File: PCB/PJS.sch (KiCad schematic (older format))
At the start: 40 parts, among them J1 HFW8R-1STE1H1LF_FFC, J10 SM02B-PASS-TBT_SwitchConnector, J2 SM02B-PASS-TBT_Connector, J3 SM02B-PASS-TBT_Connector, J4 SM02B-PASS-TBT_Connector, J5 SM02B-PASS-TBT_Connector, J6 SM02B-PASS-TBT_SwitchConnector, J7 SM02B-PASS-TBT_SwitchConnector, J8 SM02B-PASS-TBT_SwitchConnector, J9 SM02B-PASS-TBT_SwitchConnector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

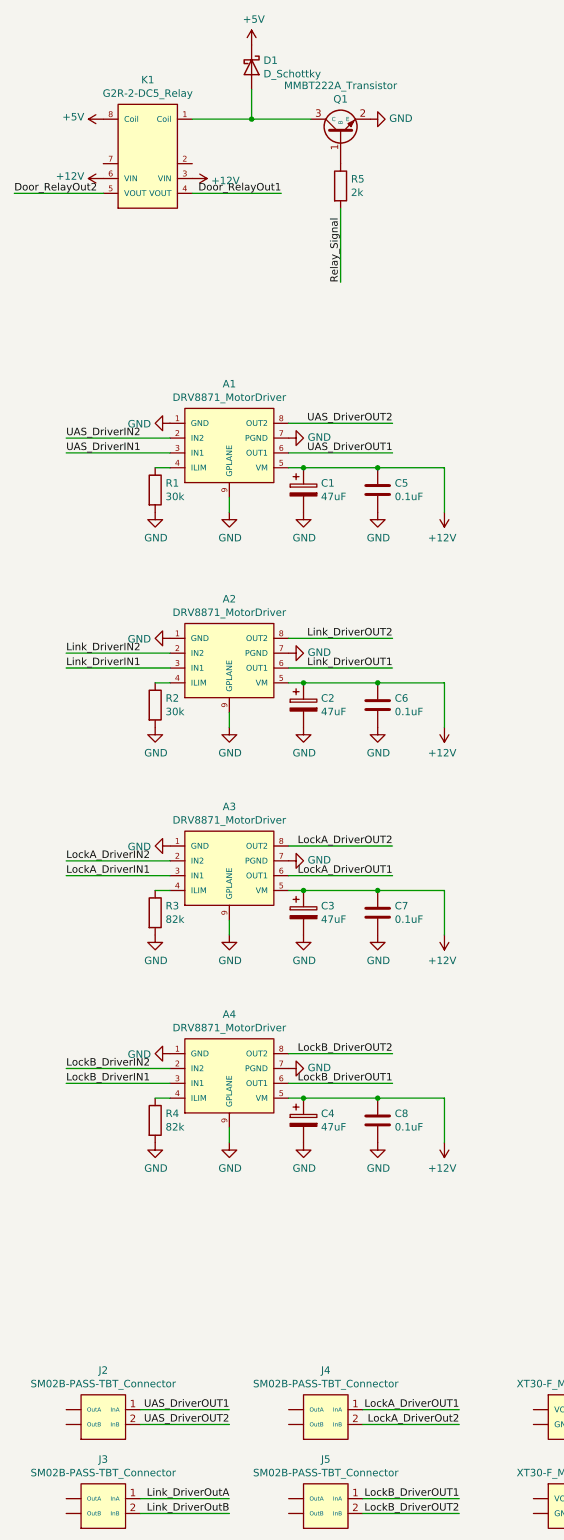
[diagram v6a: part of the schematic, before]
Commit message: Updated DRV8871 footprint
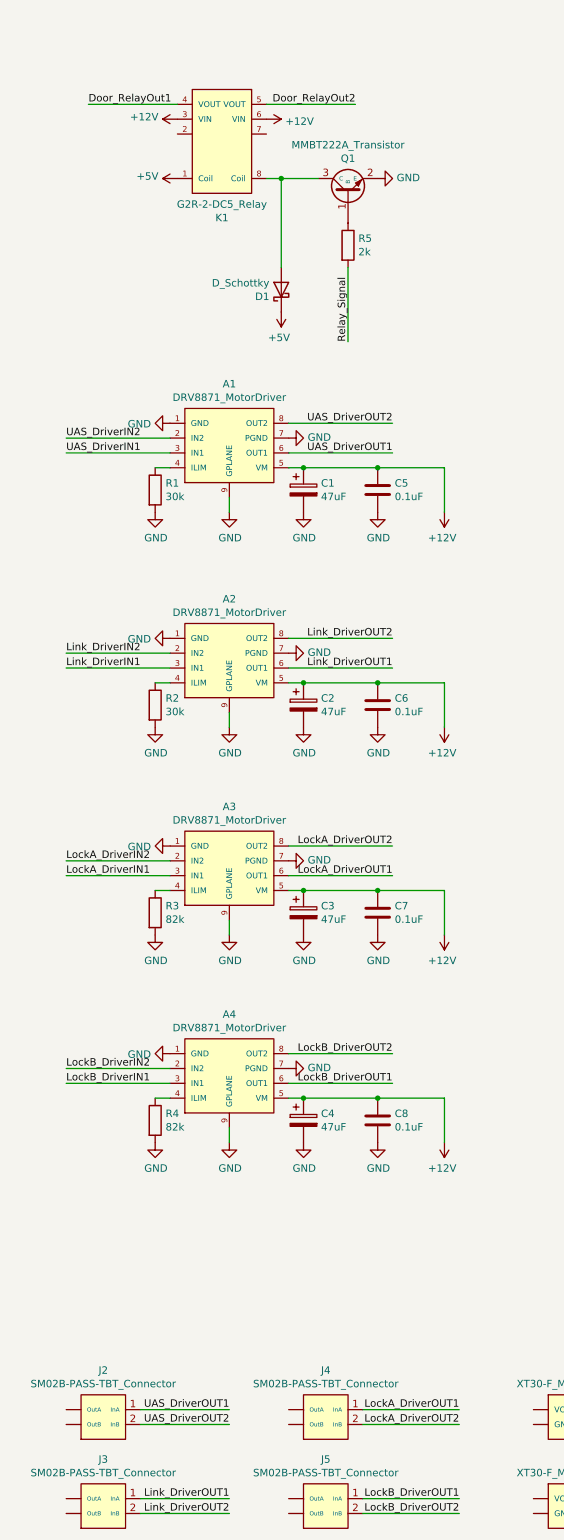
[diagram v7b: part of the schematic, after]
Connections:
- net Link_DriverOutA is gone; now on net Link_DriverOUT1: J3.1 (InA)
- net Link_DriverOutB is gone; now on net Link_DriverOUT2: J3.2 (InB)
- net LockA_DriverOut2 is gone; now on net LockA_DriverOUT2: J4.2 (InB)
- net +5V: now also K1.1 (Coil); no longer K1.8 (Coil)
- net at D1.2 (A), Q1.3 (C): now also K1.8 (Coil); no longer K1.1 (Coil)
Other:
- moved on the sheet: D1, K1, Q1, R5
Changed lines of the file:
@@
-	1    0    0    -1
-$EndComp
-$Comp
-L PJS:G2R-2-DC5_Relay K1
-U 1 1 5FCA000B
-P 1700 1950
-F 0 "K1" H 1700 2715 50  0000 C CNN
-F 1 "G2R-2-DC5_Relay" H 1700 2624 50  0000 C CNN
-F 2 "PJS:G2R-2-DC5_Relay" H 1700 2650 50  0001 C CNN
-F 3 "" H 1700 2650 50  0001 C CNN
-	1    1700 1950
 	1    0    0    -1
 $EndComp
@@
 Wire Wire Line
 	8300 8850 8800 8850
-$Comp
-L power:+12V #PWR0111
-U 1 1 5FF56403
-P 2000 1850
-F 0 "#PWR0111" H 2000 1700 50  0001 C CNN
-F 1 "+12V" V 2015 1978 50  0000 L CNN
-F 2 "" H 2000 1850 50  0001 C CNN
-F 3 "" H 2000 1850 50  0001 C CNN
-	1    2000 1850
-	0    1    1    0
-$EndComp
-$Comp
-L power:+12V #PWR0112
-U 1 1 5FF568D5
-P 1400 1850
-F 0 "#PWR0112" H 1400 1700 50  0001 C CNN
-F 1 "+12V" V 1415 1978 50  0000 L CNN
-F 2 "" H 1400 1850 50  0001 C CNN
-F 3 "" H 1400 1850 50  0001 C CNN
-	1    1400 1850
-	0    -1   -1   0
-$EndComp
 Text Label 2250 10150 2    50   ~ 0
 UAS_DriverOUT1
@@
 UAS_DriverIN2
 Text Label 2250 10750 2    50   ~ 0
-Link_DriverOutA
+Link_DriverOUT1
 Text Label 2250 10850 2    50   ~ 0
-Link_DriverOutB
+Link_DriverOUT2
 $Comp
 L power:+5V #PWR0113
@@
 Wire Wire Line
 	1650 10850 2250 10850
-Text Label 3000 2550 1    50   ~ 0
-Relay_Signal
-Wire Wire Line
-	2400 1250 2400 1450
-Wire Wire Line
-	2000 1450 2400 1450
-Connection ~ 2400 1450
 Wire Wire Line
 	6900 5650 7450 5650
@@
 Wire Wire Line
 	6900 3250 7450 3250
-$Comp
-L Device:D_Schottky D1
-U 1 1 5FFF832A
-P 2400 1100
-F 0 "D1" V 2354 1180 50  0000 L CNN
-F 1 "D_Schottky" V 2445 1180 50  0000 L CNN
-F 2 "PJS:1SS351-TB-E_Diode" H 2400 1100 50  0001 C CNN
-F 3 "~" H 2400 1100 50  0001 C CNN
-	1    2400 1100
-	0    1    1    0
-$EndComp
-$Comp
-L PJS:R R5
-U 1 1 5FFF9163
-P 3000 1900
-F 0 "R5" H 3070 1946 50  0000 L CNN
-F 1 "2k" H 3070 1855 50  0000 L CNN
-F 2 "PJS:RMCF2512FT2K00_Resistor" V 2930 1900 50  0001 C CNN
-F 3 "~" H 3000 1900 50  0001 C CNN
-	1    3000 1900
-	1    0    0    -1
-$EndComp
-Text Label 2600 1950 2    50   ~ 0
-Door_RelayOut1
-Text Label 800  1950 0    50   ~ 0
-Door_RelayOut2
-Wire Wire Line
-	2000 1950 2600 1950
-Wire Wire Line
-	800  1950 1400 1950
 $Comp
 L power:GND #PWR0117
@@
 LockA_DriverOUT1
 Text Label 3800 10250 2    50   ~ 0
-LockA_DriverOut2
+LockA_DriverOUT2
 Text Label 3800 10750 2    50   ~ 0
 LockB_DriverOUT1
 Text Label 3800 10850 2    50   ~ 0
 LockB_DriverOUT2
-Wire Wire Line
-	3000 2050 3000 2550
 Text Label 6450 4450 2    50   ~ 0
 S2_Door
@@
 Wire Wire Line
 	6450 3250 6450 3850
-Wire Wire Line
-	2400 1450 2800 1450
-$Comp
-L PJS:MMBT222A_Transistor Q1
-U 1 1 5FEF3CA0
-P 3000 1500
-F 0 "Q1" V 3185 1500 50  0000 C CNN
-F 1 "MMBT222A_Transistor" V 3276 1500 50  0000 C CNN
-F 2 "PJS:MMBT2222A_Transistor" H 3000 2100 50  0001 C CNN
-F 3 "" H 3000 2100 50  0001 C CNN
-	1    3000 1500
-	0    -1   -1   0
-$EndComp
-$Comp
-L power:GND #PWR0122
-U 1 1 5FF68CB5
-P 3200 1450
-F 0 "#PWR0122" H 3200 1200 50  0001 C CNN
-F 1 "GND" V 3205 1322 50  0000 R CNN
-F 2 "" H 3200 1450 50  0001 C CNN
-F 3 "" H 3200 1450 50  0001 C CNN
-	1    3200 1450
-	0    -1   -1   0
-$EndComp
 $Comp
 L PJS:BMP388_Altimeter A5
@@
 $EndComp
 $Comp
-L power:+5V #PWR0154
-U 1 1 5FF0C5F2
-P 2400 950
-F 0 "#PWR0154" H 2400 800 50  0001 C CNN
-F 1 "+5V" H 2415 1123 50  0000 C CNN
-F 2 "" H 2400 950 50  0001 C CNN
-F 3 "" H 2400 950 50  0001 C CNN
-	1    2400 950
-	1    0    0    -1
-$EndComp
-$Comp
-L power:+5V #PWR0155
-U 1 1 5FF0D0F3
-P 1400 1450
-F 0 "#PWR0155" H 1400 1300 50  0001 C CNN
-F 1 "+5V" V 1415 1578 50  0000 L CNN
-F 2 "" H 1400 1450 50  0001 C CNN
-F 3 "" H 1400 1450 50  0001 C CNN
-	1    1400 1450
-	0    -1   -1   0
-$EndComp
-$Comp
 L PJS:DRV8871_MotorDriver A1
 U 1 1 5FF34B84
@@
 Text Label 6900 3950 0    50   ~ 0
 LockB_DriverIN2
+$Comp
+L PJS:G2R-2-DC5_Relay K1
+U 1 1 5FCA000B
+P 2200 1350
+F 0 "K1" H 2200 2115 50  0000 C CNN
+F 1 "G2R-2-DC5_Relay" H 2200 2024 50  0000 C CNN
+F 2 "PJS:G2R-2-DC5_Relay" H 2200 2050 50  0001 C CNN
+F 3 "" H 2200 2050 50  0001 C CNN
+	1    2200 1350
+	-1   0    0    1
+$EndComp
+$Comp
+L power:+12V #PWR0111
+U 1 1 5FF56403
+P 1900 1450
+F 0 "#PWR0111" H 1900 1300 50  0001 C CNN
+F 1 "+12V" V 1915 1578 50  0000 L CNN
+F 2 "" H 1900 1450 50  0001 C CNN
+F 3 "" H 1900 1450 50  0001 C CNN
+	1    1900 1450
+	0    -1   -1   0
+$EndComp
+$Comp
+L power:+12V #PWR0112
+U 1 1 5FF568D5
+P 2500 1450
+F 0 "#PWR0112" H 2500 1300 50  0001 C CNN
+F 1 "+12V" V 2515 1578 50  0000 L CNN
+F 2 "" H 2500 1450 50  0001 C CNN
+F 3 "" H 2500 1450 50  0001 C CNN
+	1    2500 1450
+	0    1    1    0
+$EndComp
+Text Label 1300 1350 0    50   ~ 0
+Door_RelayOut1
+Wire Wire Line
+	1900 1350 1300 1350
+$Comp
+L power:+5V #PWR0155
+U 1 1 5FF0D0F3
+P 1900 1850
+F 0 "#PWR0155" H 1900 1700 50  0001 C CNN
+F 1 "+5V" V 1915 1978 50  0000 L CNN
+F 2 "" H 1900 1850 50  0001 C CNN
+F 3 "" H 1900 1850 50  0001 C CNN
+	1    1900 1850
+	0    -1   -1   0
+$EndComp
+$Comp
+L power:+5V #PWR0154
+U 1 1 5FF0C5F2
+P 2600 2750
+F 0 "#PWR0154" H 2600 2600 50  0001 C CNN
+F 1 "+5V" H 2615 2923 50  0000 C CNN
+F 2 "" H 2600 2750 50  0001 C CNN
+F 3 "" H 2600 2750 50  0001 C CNN
+	1    2600 2750
+	-1   0    0    1
+$EndComp
+$Comp
+L power:GND #PWR0122
+U 1 1 5FF68CB5
+P 3250 1850
+F 0 "#PWR0122" H 3250 1600 50  0001 C CNN
+F 1 "GND" V 3255 1722 50  0000 R CNN
+F 2 "" H 3250 1850 50  0001 C CNN
+F 3 "" H 3250 1850 50  0001 C CNN
+	1    3250 1850
+	0    -1   -1   0
+$EndComp
+Wire Wire Line
+	3100 1350 2500 1350
+Text Label 3100 1350 2    50   ~ 0
+Door_RelayOut2
+Wire Wire Line
+	3050 2450 3050 2950
+$Comp
+L PJS:R R5
+U 1 1 5FFF9163
+P 3050 2300
+F 0 "R5" H 3120 2346 50  0000 L CNN
+F 1 "2k" H 3120 2255 50  0000 L CNN
+F 2 "PJS:RMCF2512FT2K00_Resistor" V 2980 2300 50  0001 C CNN
+F 3 "~" H 3050 2300 50  0001 C CNN
+	1    3050 2300
+	1    0    0    -1
+$EndComp
+Text Label 3050 2950 1    50   ~ 0
+Relay_Signal
+$Comp
+L PJS:MMBT222A_Transistor Q1
+U 1 1 5FEF3CA0
+P 3050 1900
+F 0 "Q1" V 3235 1900 50  0000 C CNN
+F 1 "MMBT222A_Transistor" V 3326 1900 50  0000 C CNN
+F 2 "PJS:MMBT2222A_Transistor" H 3050 2500 50  0001 C CNN
+F 3 "" H 3050 2500 50  0001 C CNN
+	1    3050 1900
+	0    -1   -1   0
+$EndComp
+$Comp
+L Device:D_Schottky D1
+U 1 1 5FFF832A
+P 2600 2600
+F 0 "D1" V 2554 2680 50  0000 L CNN
+F 1 "D_Schottky" V 2645 2680 50  0000 L CNN
+F 2 "PJS:1SS351-TB-E_Diode" H 2600 2600 50  0001 C CNN
+F 3 "~" H 2600 2600 50  0001 C CNN
+	1    2600 2600
+	0    -1   -1   0
+$EndComp
+Wire Wire Line
+	2600 1850 2600 2450
+Wire Wire Line
+	2600 1850 2500 1850
+Wire Wire Line
+	2850 1850 2600 1850
+Connection ~ 2600 1850
 $EndSCHEMATC

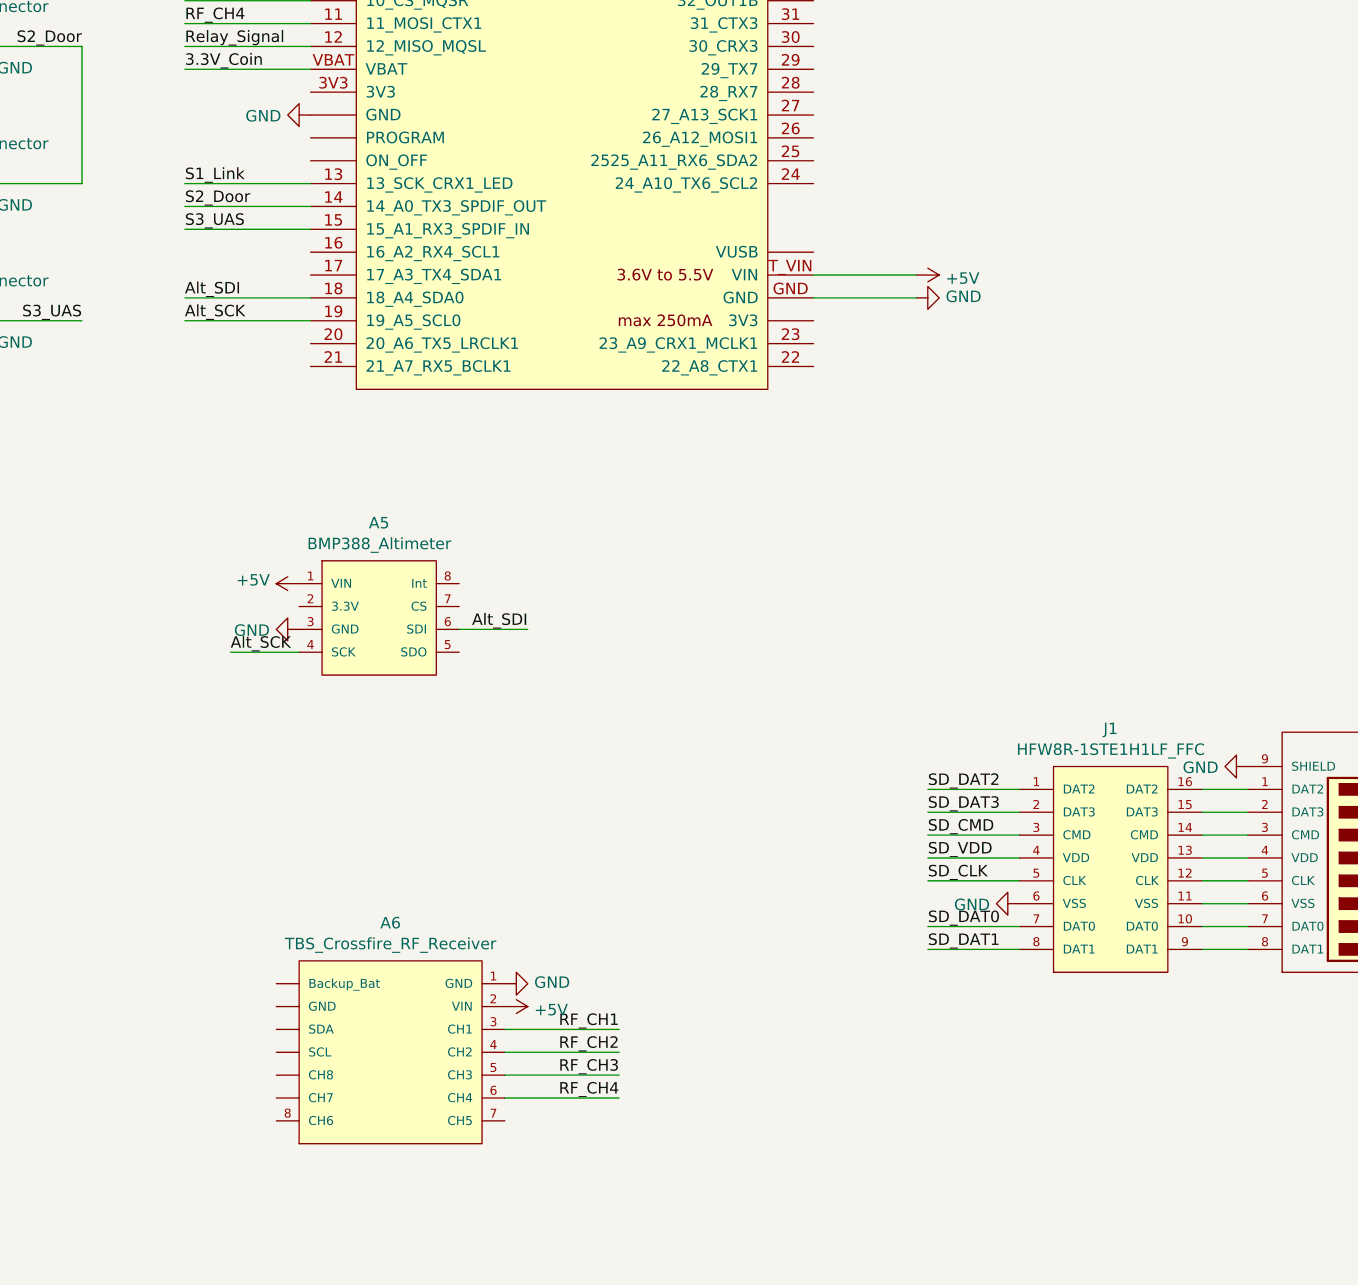
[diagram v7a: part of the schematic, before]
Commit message: PCB with TBS RF Receiver
All traces are connected. Planes and layers are not defined
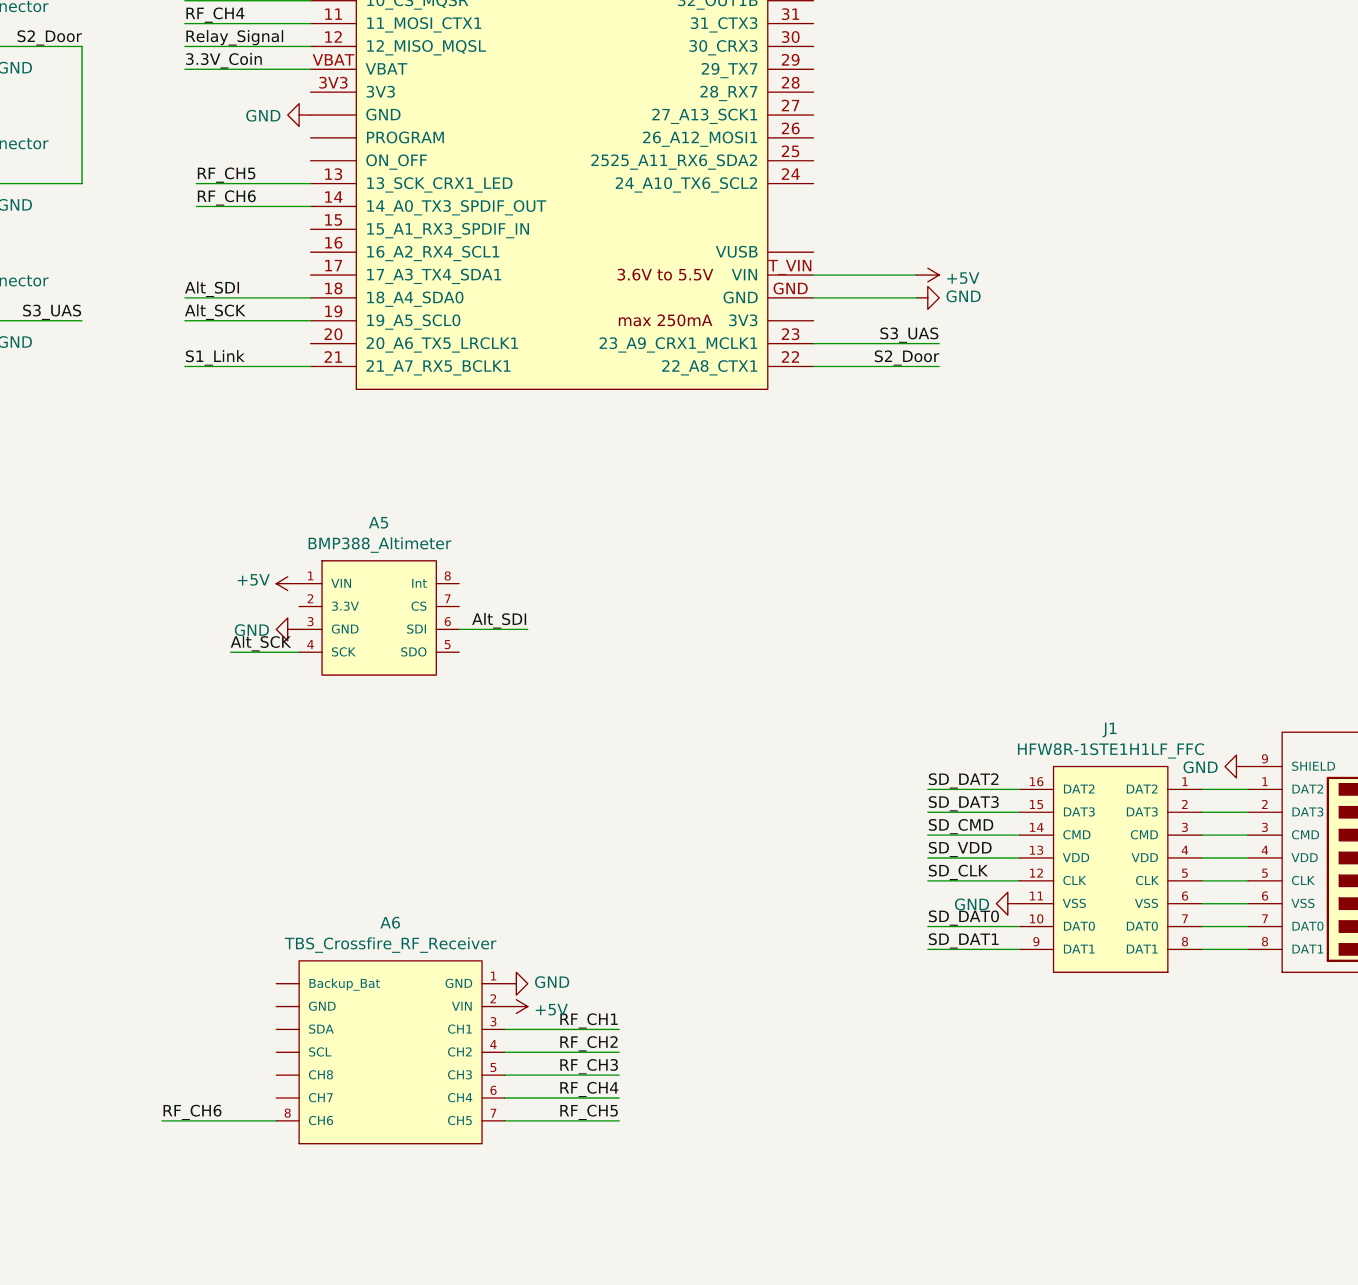
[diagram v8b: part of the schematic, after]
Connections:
- net GND: now also J1.11 (VSS); no longer J1.6 (VSS)
- net S1_Link: now also U2.21 (21_A7_RX5_BCLK1); no longer U2.13 (13_SCK_CRX1_LED)
- net S2_Door: now also U2.22 (22_A8_CTX1); no longer U2.14 (14_A0_TX3_SPDIF_OUT)
- net S3_UAS: now also U2.23 (23_A9_CRX1_MCLK1); no longer U2.15 (15_A1_RX3_SPDIF_IN)
- net SD_CLK: now also J1.12 (CLK); no longer J1.5 (CLK)
- net SD_CMD: now also J1.14 (CMD); no longer J1.3 (CMD)
- net SD_DAT0: now also J1.10 (DAT0); no longer J1.7 (DAT0)
- net SD_DAT1: now also J1.9 (DAT1); no longer J1.8 (DAT1)
- net SD_DAT2: now also J1.16 (DAT2); no longer J1.1 (DAT2)
- net SD_DAT3: now also J1.15 (DAT3); no longer J1.2 (DAT3)
- net SD_VDD: now also J1.13 (VDD); no longer J1.4 (VDD)
- net at XM1.7 (DAT0): now also J1.7 (DAT0); no longer J1.10 (DAT0)
- net at XM1.6 (VSS): now also J1.6 (VSS); no longer J1.11 (VSS)
- net at XM1.5 (CLK): now also J1.5 (CLK); no longer J1.12 (CLK)
- net at XM1.4 (VDD): now also J1.4 (VDD); no longer J1.13 (VDD)
- net at XM1.3 (CMD): now also J1.3 (CMD); no longer J1.14 (CMD)
- net at XM1.2 (DAT3): now also J1.2 (DAT3); no longer J1.15 (DAT3)
- net at XM1.1 (DAT2): now also J1.1 (DAT2); no longer J1.16 (DAT2)
- net at XM1.8 (DAT1): now also J1.8 (DAT1); no longer J1.9 (DAT1)
- net RF_CH5: now reaches A6.7 (CH5)
- net RF_CH5: now also U2.13 (13_SCK_CRX1_LED)
- net RF_CH6: now reaches A6.8 (CH6)
- net RF_CH6: now also U2.14 (14_A0_TX3_SPDIF_OUT)
